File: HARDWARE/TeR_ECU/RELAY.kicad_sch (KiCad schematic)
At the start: 5 parts, among them K1 Panasonic_ALFG2PF24, Q1 ZXMN3F30FH

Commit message: Began layout
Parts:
- removed D10: D, Diode_SMD:D_SOD-123F, symbol Device:D
- removed K1: Panasonic_ALFG2PF24, Relay_THT:Relay_SPST_Panasonic_ALFG_FormA_CircularHoles, symbol Relay:Panasonic_ALFG2PF24
- added D6: SM4007, Diode_SMD:D_MELF, symbol Diode:SM4007
- added K2: G5Q-1, Relay_THT:Relay_SPDT_Omron-G5Q-1, symbol Relay:G5Q-1
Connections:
- net +24V: now also D6.1 (K), K2.5
- net SL_IN: now also K2.2
- net SL_OUT: now also K2.3
- net at Q1.3 (D): now also D6.2 (A), K2.1
- no-connect marks 0 -> 1
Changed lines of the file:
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@@
 		(color 0 0 0 0)
 	)
+	(no_connect
+		(at 119.38 77.47)
+	)
 	(wire
 		(pts
@@
 	(wire
 		(pts
-			(xy 127 95.25) (xy 138.43 95.25)
+			(xy 127 95.25) (xy 143.51 95.25)
 		)
 		(stroke
@@
 	(wire
 		(pts
-			(xy 138.43 73.66) (xy 127 73.66)
+			(xy 143.51 73.66) (xy 127 73.66)
 		)
 		(stroke
@@
 	(wire
 		(pts
-			(xy 138.43 81.28) (xy 138.43 73.66)
+			(xy 143.51 81.28) (xy 143.51 73.66)
 		)
 		(stroke
@@
 	(wire
 		(pts
-			(xy 138.43 88.9) (xy 138.43 95.25)
+			(xy 143.51 88.9) (xy 143.51 95.25)
 		)
 		(stroke
@@
 	)
 	(symbol
-		(lib_id "Device:D")
-		(at 138.43 85.09 270)
+		(lib_id "Relay:G5Q-1")
+		(at 121.92 85.09 0)
+		(mirror y)
 		(unit 1)
 		(exclude_from_sim no)
@@
 		(dnp no)
 		(fields_autoplaced yes)
-		(property "Reference" "D10"
-			(at 140.97 83.82 90)
+		(property "Reference" "K2"
+			(at 133.35 83.8199 0)
+			(effects
+				(font
+					(size 1.27 1.27)
+				)
+				(justify right)
+			)
+		)
+		(property "Value" "G5Q-1"
+			(at 133.35 86.3599 0)
+			(effects
+				(font
+					(size 1.27 1.27)
+				)
+				(justify right)
+			)
+		)
+		(property "Footprint" "Relay_THT:Relay_SPDT_Omron-G5Q-1"
+			(at 110.49 86.36 0)
 			(effects
 				(font
@@
 				)
 				(justify left)
-			)
-		)
-		(property "Value" "D"
-			(at 140.97 86.36 90)
+				(hide yes)
+			)
+		)
+		(property "Datasheet" "https://www.omron.com/ecb/products/pdf/en-g5q.pdf"
+			(at 121.92 85.09 0)
 			(effects
 				(font
@@
 				)
 				(justify left)
-			)
-		)
-		(property "Footprint" "Diode_SMD:D_SOD-123F"
-			(at 138.43 85.09 0)
-			(effects
-				(font
-					(size 1.27 1.27)
-				)
-				(hide yes)
-			)
-		)
-		(property "Datasheet" "~"
-			(at 138.43 85.09 0)
-			(effects
-				(font
-					(size 1.27 1.27)
-				)
-				(hide yes)
-			)
-		)
-		(property "Description" ""
-			(at 138.43 85.09 0)
-			(effects
-				(font
-					(size 1.27 1.27)
-				)
-				(hide yes)
-			)
-		)
-		(property "Sim.Device" "D"
-			(at 138.43 85.09 0)
-			(effects
-				(font
-					(size 1.27 1.27)
-				)
-				(hide yes)
-			)
-		)
-		(property "Sim.Pins" "1=K 2=A"
-			(at 138.43 85.09 0)
-			(effects
-				(font
-					(size 1.27 1.27)
-				)
-				(hide yes)
-			)
+				(hide yes)
+			)
+		)
+		(property "Description" "Omron G5G relay, Miniature Single Pole, SPDT, 10A"
+			(at 121.92 85.09 0)
+			(effects
+				(font
+					(size 1.27 1.27)
+				)
+				(hide yes)
+			)
+		)
+		(pin "2"
 		)
 		(pin "1"
 		)
-		(pin "2"
+		(pin "5"
+		)
+		(pin "3"
+		)
+		(pin "4"
 		)
 		(instances
-			(project "TER_LVBMS"
-				(path "/427cf896-f780-4d4b-86ef-f90b31c1397d/8aa3c5f8-2a3f-44a9-920d-01bf32a384b0"
-					(reference "D10")
-					(unit 1)
-				)
-			)
-			(project "TER_LVBMS"
+			(project ""
 				(path "/84413845-c4f3-4743-bcd2-a67649c90902/adfb2d76-93cc-4bc6-a50d-e4f688c5252c"
-					(reference "D31")
+					(reference "K2")
 					(unit 1)
 				)
@@
 	)
 	(symbol
+		(lib_id "Diode:SM4007")
+		(at 143.51 85.09 270)
+		(unit 1)
+		(exclude_from_sim no)
+		(in_bom yes)
+		(on_board yes)
+		(dnp no)
+		(fields_autoplaced yes)
+		(property "Reference" "D6"
+			(at 146.05 83.8199 90)
+			(effects
+				(font
+					(size 1.27 1.27)
+				)
+				(justify left)
+			)
+		)
+		(property "Value" "SM4007"
+			(at 146.05 86.3599 90)
+			(effects
+				(font
+					(size 1.27 1.27)
+				)
+				(justify left)
+			)
+		)
+		(property "Footprint" "Diode_SMD:D_MELF"
+			(at 139.065 85.09 0)
+			(effects
+				(font
+					(size 1.27 1.27)
+				)
+				(hide yes)
+			)
+		)
+		(property "Datasheet" "http://cdn-reichelt.de/documents/datenblatt/A400/SMD1N400%23DIO.pdf"
+			(at 143.51 85.09 0)
+			(effects
+				(font
+					(size 1.27 1.27)
+				)
+				(hide yes)
+			)
+		)
+		(property "Description" "1000V 1A General Purpose Rectifier Diode, MELF"
+			(at 143.51 85.09 0)
+			(effects
+				(font
+					(size 1.27 1.27)
+				)
+				(hide yes)
+			)
+		)
+		(property "Sim.Device" "D"
+			(at 143.51 85.09 0)
+			(effects
+				(font
+					(size 1.27 1.27)
+				)
+				(hide yes)
+			)
+		)
+		(property "Sim.Pins" "1=K 2=A"
+			(at 143.51 85.09 0)
+			(effects
+				(font
+					(size 1.27 1.27)
+				)
+				(hide yes)
+			)
+		)
+		(pin "1"
+		)
+		(pin "2"
+		)
+		(instances
+			(project ""
+				(path "/84413845-c4f3-4743-bcd2-a67649c90902/adfb2d76-93cc-4bc6-a50d-e4f688c5252c"
+					(reference "D6")
+					(unit 1)
+				)
+			)
+		)
+	)
+	(symbol
 		(lib_id "Device:R")
 		(at 110.49 110.49 90)
@@
 					(unit 1)
 				)
-			)
-		)
-	)
-	(symbol
-		(lib_id "Relay:Panasonic_ALFG2PF24")
-		(at 121.92 85.09 0)
-		(mirror y)
-		(unit 1)
-		(exclude_from_sim no)
-		(in_bom yes)
-		(on_board yes)
-		(dnp no)
-		(property "Reference" "K1"
-			(at 110.49 83.8199 0)
-			(effects
-				(font
-					(size 1.27 1.27)
-				)
-				(justify left)
-			)
-		)
-		(property "Value" "Panasonic_ALFG2PF24"
-			(at 110.49 86.3599 0)
-			(effects
-				(font
-					(size 1.27 1.27)
-				)
-				(justify left)
-			)
-		)
-		(property "Footprint" "Relay_THT:Relay_SPST_Panasonic_ALFG_FormA_CircularHoles"
-			(at 89.662 85.852 0)
-			(effects
-				(font
-					(size 1.27 1.27)
-				)
-				(hide yes)
-			)
-		)
-		(property "Datasheet" "https://www3.panasonic.biz/ac/e_download/control/relay/power/catalog/mech_eng_lfg.pdf"
-			(at 121.92 85.09 0)
-			(effects
-				(font
-					(size 1.27 1.27)
-				)
-				(hide yes)
-			)
-		)
-		(property "Description" "24V DC, High Capacity, 31A, Contact Gap 1.5mm, ALFG_FormA"
-			(at 121.92 85.09 0)
-			(effects
-				(font
-					(size 1.27 1.27)
-				)
-				(hide yes)
-			)
-		)
-		(pin "11"
-		)
-		(pin "A2"
-		)
-		(pin "A1"
-		)
-		(pin "14"
-		)
-		(instances
-			(project "TER_LVBMS"
-				(path "/427cf896-f780-4d4b-86ef-f90b31c1397d/8aa3c5f8-2a3f-44a9-920d-01bf32a384b0"
-					(reference "K1")
-					(unit 1)
-				)
-			)
-			(project "TER_LVBMS"
-				(path "/84413845-c4f3-4743-bcd2-a67649c90902/adfb2d76-93cc-4bc6-a50d-e4f688c5252c"
-					(reference "K1")
-					(unit 1)
-				)

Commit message: First layout prototype
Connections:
- net SL_IN renamed SC_IN
- net SL_OUT renamed SC_OUT
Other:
- note added: "El peak insrush current de los coils de los AIR es 3.8Amps luego el switch current del relé debería ser capáz de soportarlos. Este lo hace"
- moved on the sheet: D6, K2, Q1, R27, R28

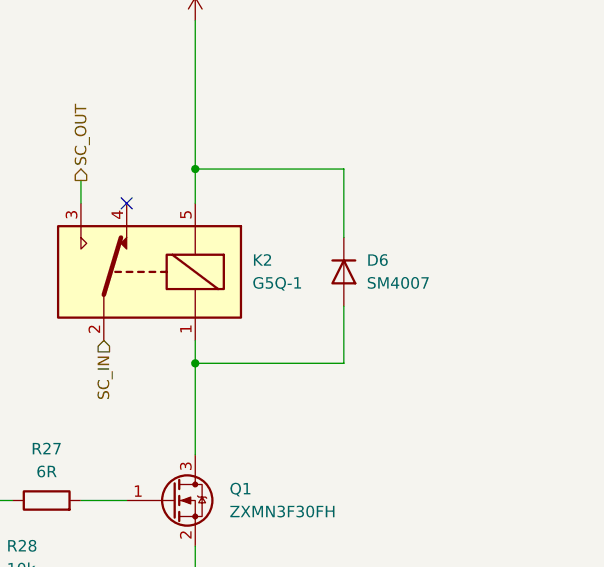
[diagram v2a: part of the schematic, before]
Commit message: Added Diode to clamp usb pwr
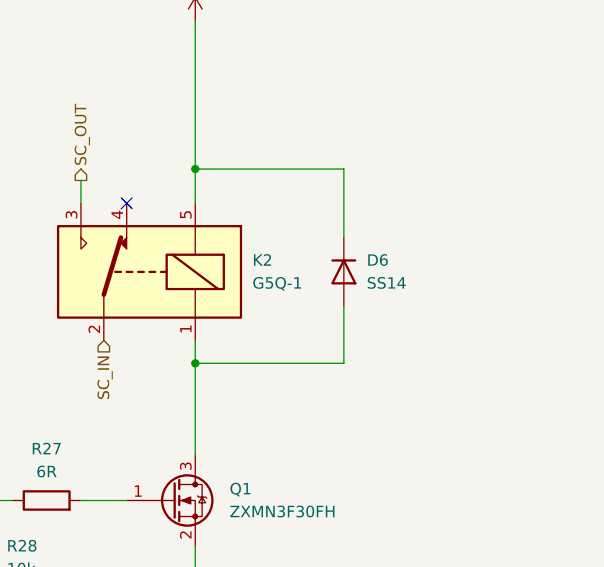
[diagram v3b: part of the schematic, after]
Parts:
- D6: value SM4007 -> SS14; footprint Diode_SMD:D_MELF -> Diode_SMD:D_SOD-123
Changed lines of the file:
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@@
 			)
 		)
-		(property "Value" "SM4007"
+		(property "Value" "SS14"
 			(at 167.64 80.0099 90)
 			(effects
@@
 			)
 		)
-		(property "Footprint" "Diode_SMD:D_MELF"
+		(property "Footprint" "Diode_SMD:D_SOD-123"
 			(at 160.655 78.74 0)
 			(effects
